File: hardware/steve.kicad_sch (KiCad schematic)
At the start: 33 parts, among them J1 Conn_ARM_JTAG_SWD_10, J4 Screw_Terminal_01x04, J5 USB_C_Receptacle_16P, SW1 SW_SPST, SW2 SW_SPST, U1 STM32F407VGTx, U3 TLV1117LV33DCYR, Y1 12MHz, Y2 32.768kHz

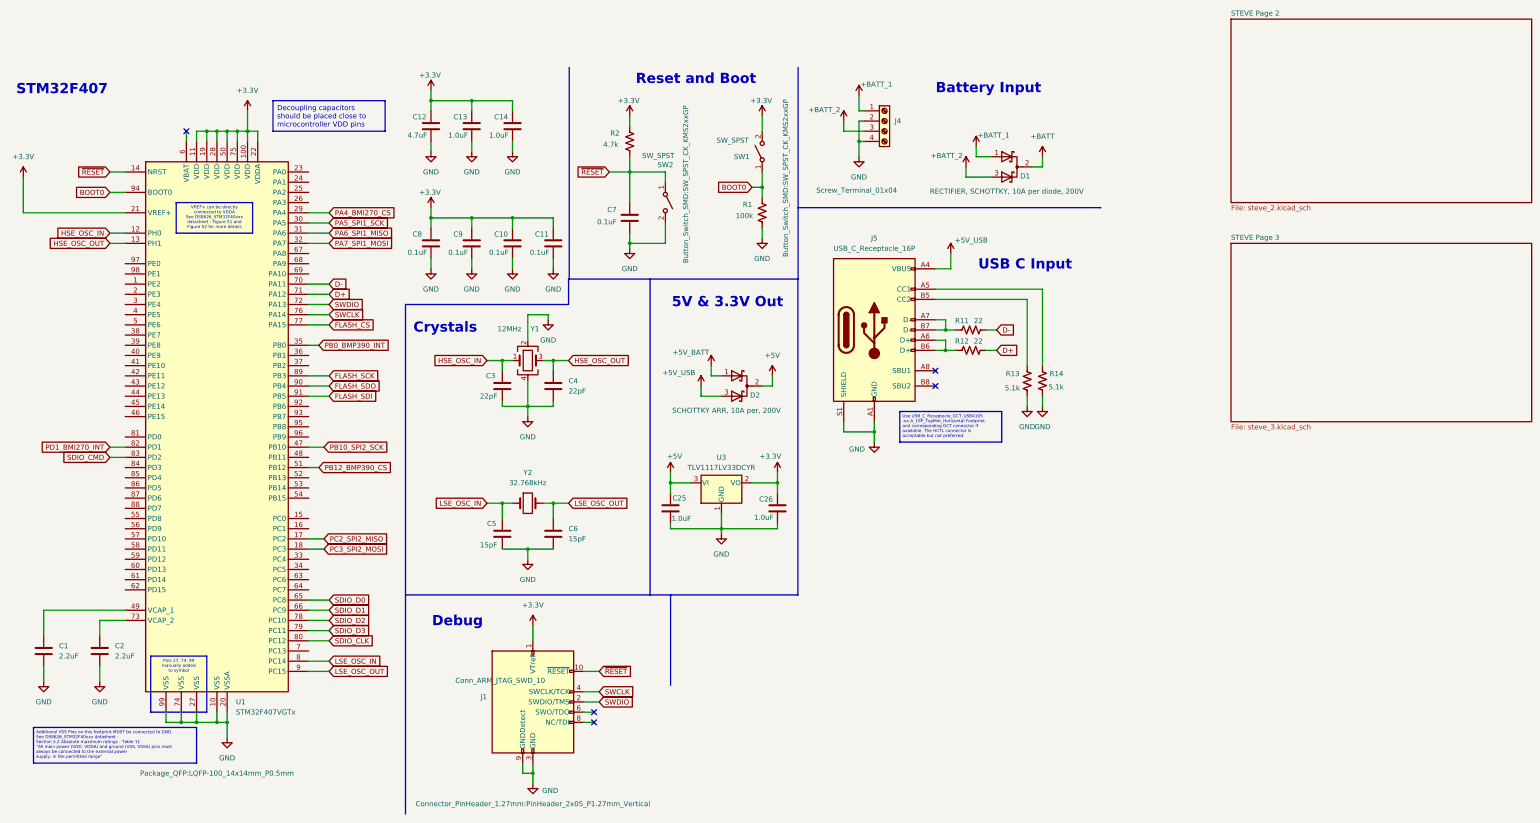
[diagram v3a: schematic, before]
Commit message: Add components to schematic; fix existing ones
Added additional components to schematic such as IO connectors. Replaced the 10A TO-263-2 diode rectifiers with much smaller 5A ones.
Other various fixes.
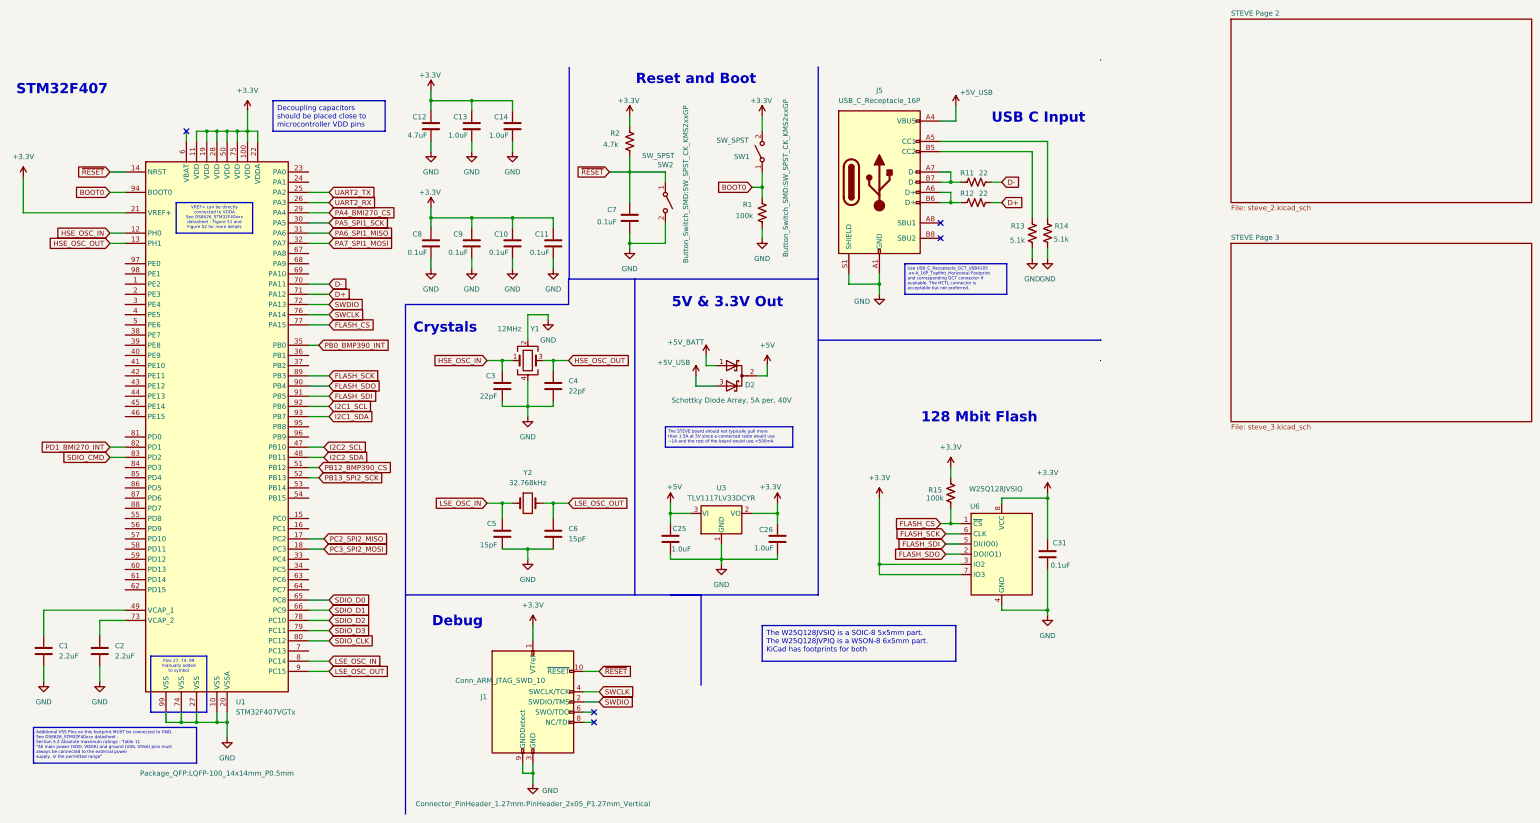
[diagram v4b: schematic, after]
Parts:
- removed D1: RECTIFIER, SCHOTTKY, 10A per diode, 200V, Package_TO_SOT_SMD:TO-263-2, symbol Device:D_Schottky_Dual_CommonCathode_AKA_Parallel
- removed J4: Screw_Terminal_01x04, TerminalBlock_Phoenix:TerminalBlock_Phoenix_PT-1,5-4-5.0-H_1x04_P5.00mm_Horizontal, symbol Connector:Screw_Terminal_01x04
- added C31: 0.1uF, Capacitor_SMD:C_0603_1608Metric, symbol Device:C
- added R15: 100k, Resistor_SMD:R_0603_1608Metric, symbol Device:R_US
- added U6: W25Q128JVSIQ, Package_SO:SOIC-8_5.23x5.23mm_P1.27mm, symbol Memory_Flash:W25Q128JVS
- D2: value SCHOTTKY ARR, 10A per, 200V -> Schottky Diode Array, 5A per, 40V; footprint Package_TO_SOT_SMD:TO-263-2 -> Imported_Footprints:PDS1040CTL-13_PowerDI-5
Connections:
- net +3.3V: now also C31.1, R15.1, U6.3 (IO2), U6.7 (IO3), U6.8 (VCC)
- net FLASH_CS: now also R15.2, U6.1 (~{CS})
- net FLASH_SCK: now also U6.6 (CLK)
- net FLASH_SDI: now also U6.5 (DI(IO0))
- net FLASH_SDO: now also U6.2 (DO(IO1))
- net GND: now also C31.2, U6.4 (GND)
- net UART2_TX: now reaches U1.25 (PA2)
- net UART2_RX: now reaches U1.26 (PA3)
- net I2C2_SDA: now reaches U1.48 (PB11)
- net PB13_SPI2_SCK: now reaches U1.52 (PB13)
- net I2C1_SCL: now reaches U1.92 (PB6)
- net I2C1_SDA: now reaches U1.93 (PB7)
- net PB10_SPI2_SCK renamed I2C2_SCL
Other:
- note added: "128 Mbit Flash"
- note removed: "Battery Input"
- moved on the sheet: C25, C26, J5, R11, R12, R13, R14, U3

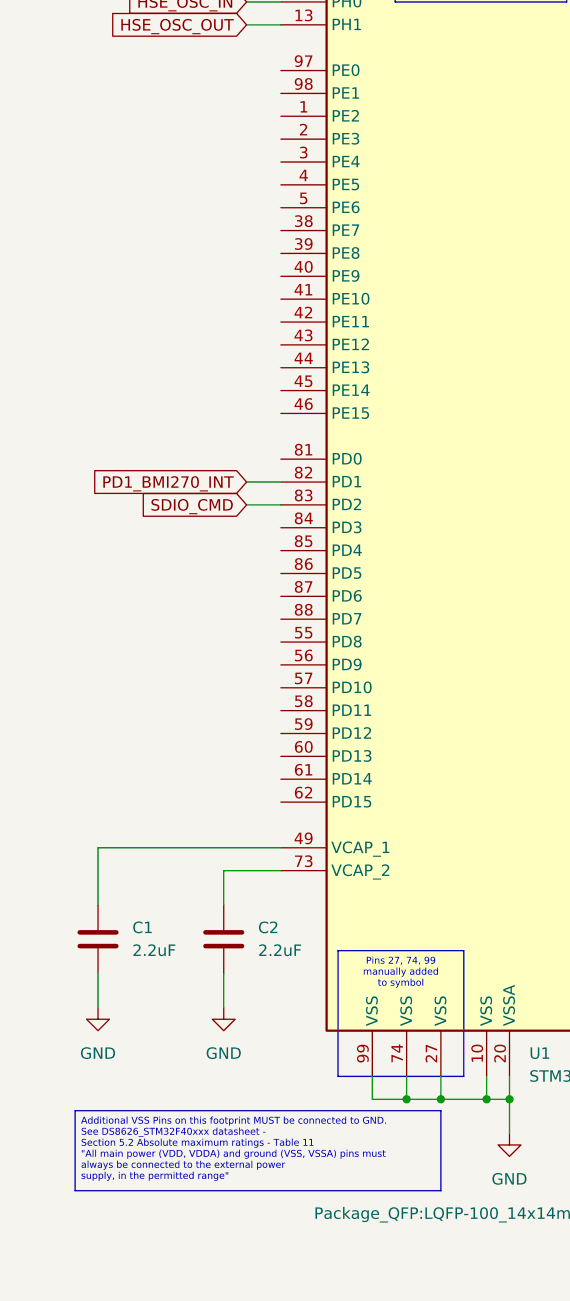
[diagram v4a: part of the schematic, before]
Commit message: Added buzzer and LEDs to schematic
Added buzzer and LEDs (4 regular and 2 WS2812B) to schematic. Minor schematic fixes such as PMIC enable pin voltage divider.
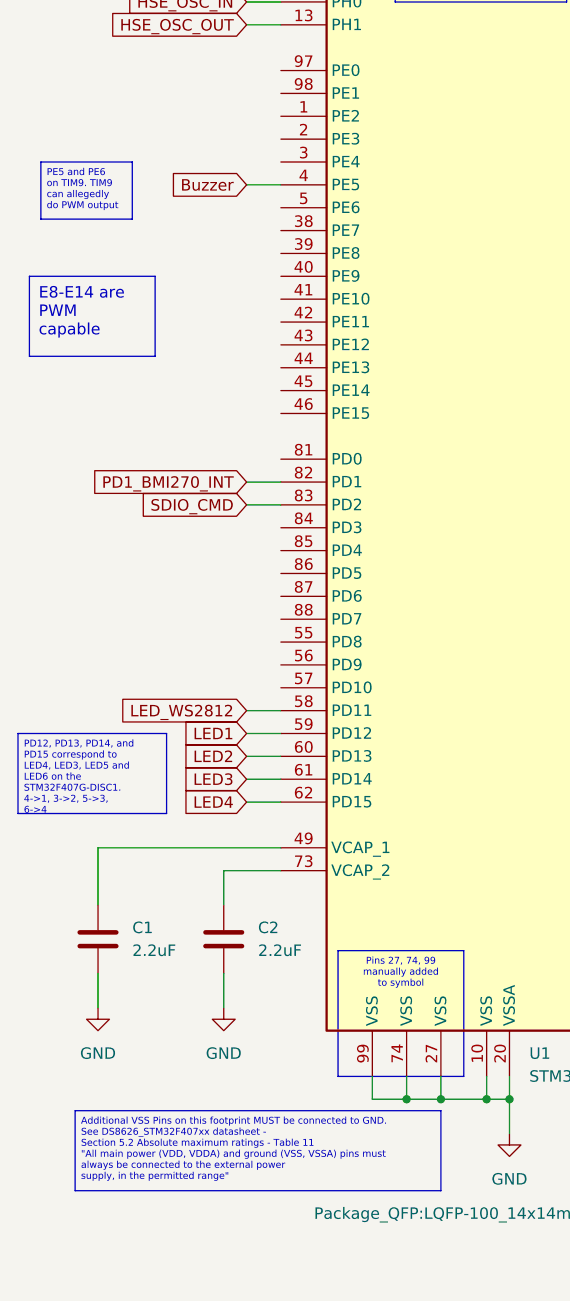
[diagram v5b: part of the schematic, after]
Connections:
- net Buzzer: now reaches U1.4 (PE5)
- net LED_WS2812: now reaches U1.58 (PD11)
- net LED1: now reaches U1.59 (PD12)
- net LED2: now reaches U1.60 (PD13)
- net LED3: now reaches U1.61 (PD14)
- net LED4: now reaches U1.62 (PD15)
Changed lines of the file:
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@@
 	(wire
 		(pts
+			(xy 38.1 139.7) (xy 41.91 139.7)
+		)
+		(stroke
+			(width 0)
+			(type default)
+		)
+	)
+	(wire
+		(pts
 			(xy 245.11 25.4) (xy 248.92 25.4)
 		)
@@
 	(wire
 		(pts
+			(xy 38.1 73.66) (xy 41.91 73.66)
+		)
+		(stroke
+			(width 0)
+			(type default)
+		)
+	)
+	(wire
+		(pts
 			(xy 138.43 52.07) (xy 138.43 49.53)
 		)
@@
 	(wire
 		(pts
+			(xy 38.1 132.08) (xy 41.91 132.08)
+		)
+		(stroke
+			(width 0)
+			(type default)
+		)
+	)
+	(wire
+		(pts
 			(xy 201.93 88.9) (xy 201.93 86.36)
 		)
@@
 	(wire
 		(pts
+			(xy 38.1 134.62) (xy 41.91 134.62)
+		)
+		(stroke
+			(width 0)
+			(type default)
+		)
+	)
+	(wire
+		(pts
 			(xy 229.87 119.38) (xy 229.87 135.89)
 		)
@@
 	(wire
 		(pts
+			(xy 38.1 137.16) (xy 41.91 137.16)
+		)
+		(stroke
+			(width 0)
+			(type default)
+		)
+	)
+	(wire
+		(pts
 			(xy 21.59 147.32) (xy 21.59 153.67)
 		)
@@
 	(wire
 		(pts
+			(xy 38.1 142.24) (xy 41.91 142.24)
+		)
+		(stroke
+			(width 0)
+			(type default)
+		)
+	)
+	(wire
+		(pts
 			(xy 62.23 27.94) (xy 62.23 30.48)
 		)
@@
 		)
 	)
+	(text_box "E8-E14 are PWM capable"
+		(exclude_from_sim no)
+		(at 13.97 83.82 0)
+		(size 13.97 8.89)
+		(stroke
+			(width 0)
+			(type default)
+		)
+		(fill
+			(type none)
+		)
+		(effects
+			(font
+				(size 1.27 1.27)
+			)
+			(justify left top)
+		)
+	)
 	(text_box "VREF+ can be directly \nconnected to VDDA\nSee DS8626_STM32F40xxx \ndatasheet - Figure 51 and \nFigure 52 for more details"
 		(exclude_from_sim no)
@@
 		)
 	)
-	(text_box "Additional VSS Pins on this footprint MUST be connected to GND.\nSee DS8626_STM32F40xxx datasheet - \nSection 5.2 Absolute maximum ratings - Table 11\n\"All main power (VDD, VDDA) and ground (VSS, VSSA) pins must \nalways be connected to the external power\nsupply, in the permitted range\""
+	(text_box "PD12, PD13, PD14, and PD15 correspond to LED4, LED3, LED5 and LED6 on the STM32F407G-DISC1. 4->1, 3->2, 5->3, 6->4"
+		(exclude_from_sim no)
+		(at 12.7 134.62 0)
+		(size 16.51 8.89)
+		(stroke
+			(width 0)
+			(type default)
+		)
+		(fill
+			(type none)
+		)
+		(effects
+			(font
+				(size 0.762 0.762)
+			)
+			(justify left top)
+		)
+	)
+	(text_box "Additional VSS Pins on this footprint MUST be connected to GND.\nSee DS8626_STM32F407xx datasheet - \nSection 5.2 Absolute maximum ratings - Table 11\n\"All main power (VDD, VDDA) and ground (VSS, VSSA) pins must \nalways be connected to the external power\nsupply, in the permitted range\""
 		(exclude_from_sim no)
 		(at 19.05 176.53 0)
@@
 		)
 	)
+	(text_box "PE5 and PE6 on TIM9. TIM9 can allegedly do PWM output"
+		(exclude_from_sim no)
+		(at 15.24 71.12 0)
+		(size 10.16 6.35)
+		(stroke
+			(width 0)
+			(type default)
+		)
+		(fill
+			(type none)
+		)
+		(effects
+			(font
+				(size 0.762 0.762)
+			)
+			(justify left top)
+		)
+	)
 	(text "128 Mbit Flash"
 		(exclude_from_sim no)
@@
 		)
 	)
+	(global_label "Buzzer"
+		(shape input)
+		(at 38.1 73.66 180)
+		(fields_autoplaced yes)
+		(effects
+			(font
+				(size 1.27 1.27)
+			)
+			(justify right)
+		)
+		(property "Intersheetrefs" "${INTERSHEET_REFS}"
+			(at 28.7648 73.66 0)
+			(effects
+				(font
+					(size 1.27 1.27)
+				)
+				(justify right)
+				(hide yes)
+			)
+		)
+	)
 	(global_label "~{RESET}"
 		(shape input)
@@
 		)
 	)
+	(global_label "LED3"
+		(shape input)
+		(at 38.1 139.7 180)
+		(fields_autoplaced yes)
+		(effects
+			(font
+				(size 1.27 1.27)
+			)
+			(justify right)
+		)
+		(property "Intersheetrefs" "${INTERSHEET_REFS}"
+			(at 30.4582 139.7 0)
+			(effects
+				(font
+					(size 1.27 1.27)
+				)
+				(justify right)
+				(hide yes)
+			)
+		)
+	)
+	(global_label "LED2"
+		(shape input)
+		(at 38.1 137.16 180)
+		(fields_autoplaced yes)
+		(effects
+			(font
+				(size 1.27 1.27)
+			)
+			(justify right)
+		)
+		(property "Intersheetrefs" "${INTERSHEET_REFS}"
+			(at 30.4582 137.16 0)
+			(effects
+				(font
+					(size 1.27 1.27)
+				)
+				(justify right)
+				(hide yes)
+			)
+		)
+	)
 	(global_label "HSE_OSC_IN"
 		(shape input)
@@
 		)
 	)
+	(global_label "LED1"
+		(shape input)
+		(at 38.1 134.62 180)
+		(fields_autoplaced yes)
+		(effects
+			(font
+				(size 1.27 1.27)
+			)
+			(justify right)
+		)
+		(property "Intersheetrefs" "${INTERSHEET_REFS}"
+			(at 30.4582 134.62 0)
+			(effects
+				(font
+					(size 1.27 1.27)
+				)
+				(justify right)
+				(hide yes)
+			)
+		)
+	)
 	(global_label "HSE_OSC_IN"
 		(shape input)
@@
 		)
 	)
+	(global_label "LED_WS2812"
+		(shape input)
+		(at 38.1 132.08 180)
+		(fields_autoplaced yes)
+		(effects
+			(font
+				(size 1.27 1.27)
+			)
+			(justify right)
+		)
+		(property "Intersheetrefs" "${INTERSHEET_REFS}"
+			(at 23.2012 132.08 0)
+			(effects
+				(font
+					(size 1.27 1.27)
+				)
+				(justify right)
+				(hide yes)
+			)
+		)
+	)
 	(global_label "PB13_SPI2_SCK"
 		(shape input)
@@
 				(hide yes)
 			)
+		)
+	)
+	(global_label "LED4"
+		(shape input)
+		(at 38.1 142.24 180)
+		(fields_autoplaced yes)
+		(effects
+			(font
+				(size 1.27 1.27)
+			)
+			(justify right)
+		)
+		(property "Intersheetrefs" "${INTERSHEET_REFS}"
+			(at 30.4582 142.24 0)
+			(effects
+				(font
+					(size 1.27 1.27)
+				)
+				(justify right)
+				(hide yes)
+			)
